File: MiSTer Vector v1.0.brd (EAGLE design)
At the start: 60.1 x 63.9 mm, 39 parts, among them CON2 22-23-2021, IC1 74HC00D, IC2 TL084, IC3 TL084, IC7 MAX6105, U1 MCP4922, U2 MCP4922, U3 MCP4922, U8 VASD1-SIP

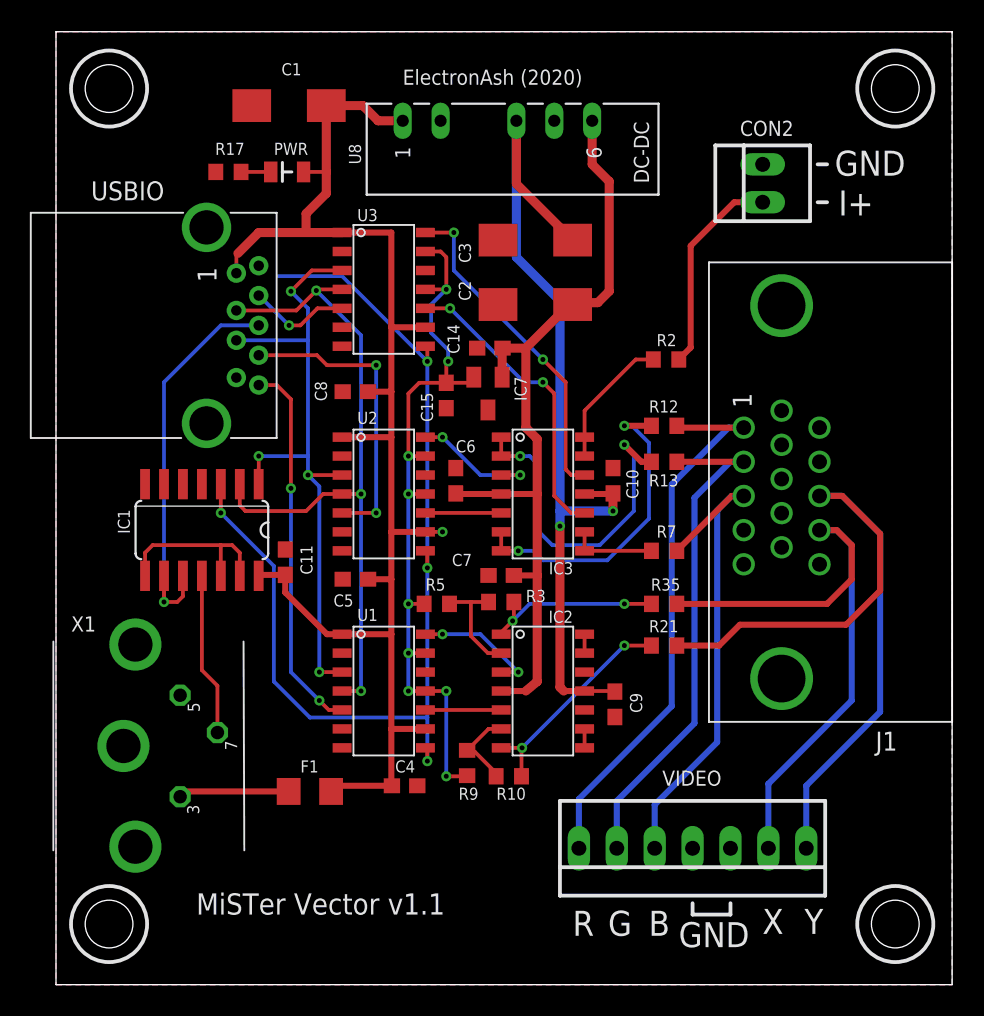
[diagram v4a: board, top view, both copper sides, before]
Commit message: changed DB15 to DB25, for use with laser projectors
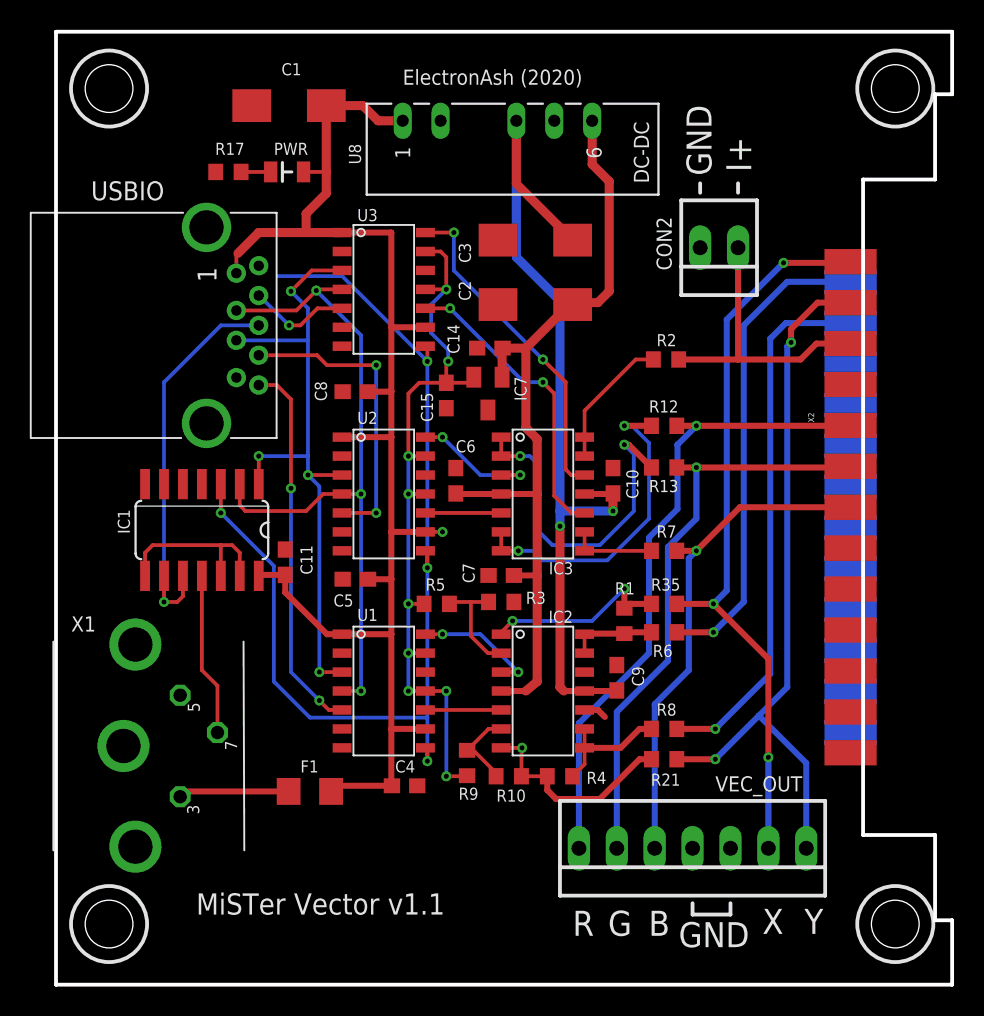
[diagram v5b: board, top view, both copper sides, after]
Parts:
- removed J1: (no value), con-wurth:618015330923
- added R1, R4: 10K, resistor:R0603
- added R6, R8: 75R, resistor:R0603
- added X2: ILDA 25 Pin, SparkFun:F25D
- moved R21 7.62 mm to (40.8, 15.1)
- moved CON2 5.21 mm to (44.5, 49.4), turned to 180 degrees
- moved C9 1.78 mm to (37.6, 20.6), turned to 270 degrees
- moved R13 0.38 mm to (40.8, 34.7)
- renumbered VIDEO to VEC_OUT
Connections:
- new net INTERLOCK: X2.17, X2.4
- new net SHUTTER: X2.13
- new net X-: R6.2, X2.14
- new net Y-: R8.2, X2.15
- net B+: now also X2.7; no longer J1.3
- net G+: now also X2.6; no longer J1.2
- net GND: now also X2.16, X2.18, X2.19, X2.20, X2.21, X2.22, X2.23, X2.25; no longer J1.10, J1.5, J1.6, J1.7, J1.8, J1.SHELL, J1.SHELL1
- net I+: now also X2.3
- net N$1: now also R1.1
- net N$2: now also R4.1
- net N$4: now also R4.2, R8.1
- net N$5: now also R1.2, R6.1
- net R+: now also X2.5; no longer J1.1
- net X+: now also X2.1; no longer J1.14
- net Y+: now also X2.2; no longer J1.13
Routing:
- net Y-: track 0.00 -> 36.1 mm, vias 0 -> 1
- net X-: track 0.00 -> 32.3 mm, vias 0 -> 1
- net N$4: track 1.27 -> 8.52 mm
- net X+: track 42.5 -> 49.7 mm, vias 0 -> 3
- net I+: track 14.0 -> 19.5 mm
- net R+: track 37.9 -> 43.2 mm, vias 0 -> 1
- net G+: track 34.4 -> 39.4 mm, vias 0 -> 1
- net N$5: track 1.27 -> 5.81 mm
- net Y+: track 52.3 -> 48.4 mm, vias 0 -> 2
- net GND: track 0.00 -> 1.55 mm
- net B+: track 32.6 -> 34.0 mm, vias 0 -> 1
- net N$1: track 12.3 -> 12.8 mm
- net N$2: track 14.8 -> 14.3 mm, vias 2 -> 1
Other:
- outline, holes or cut-outs redrawn

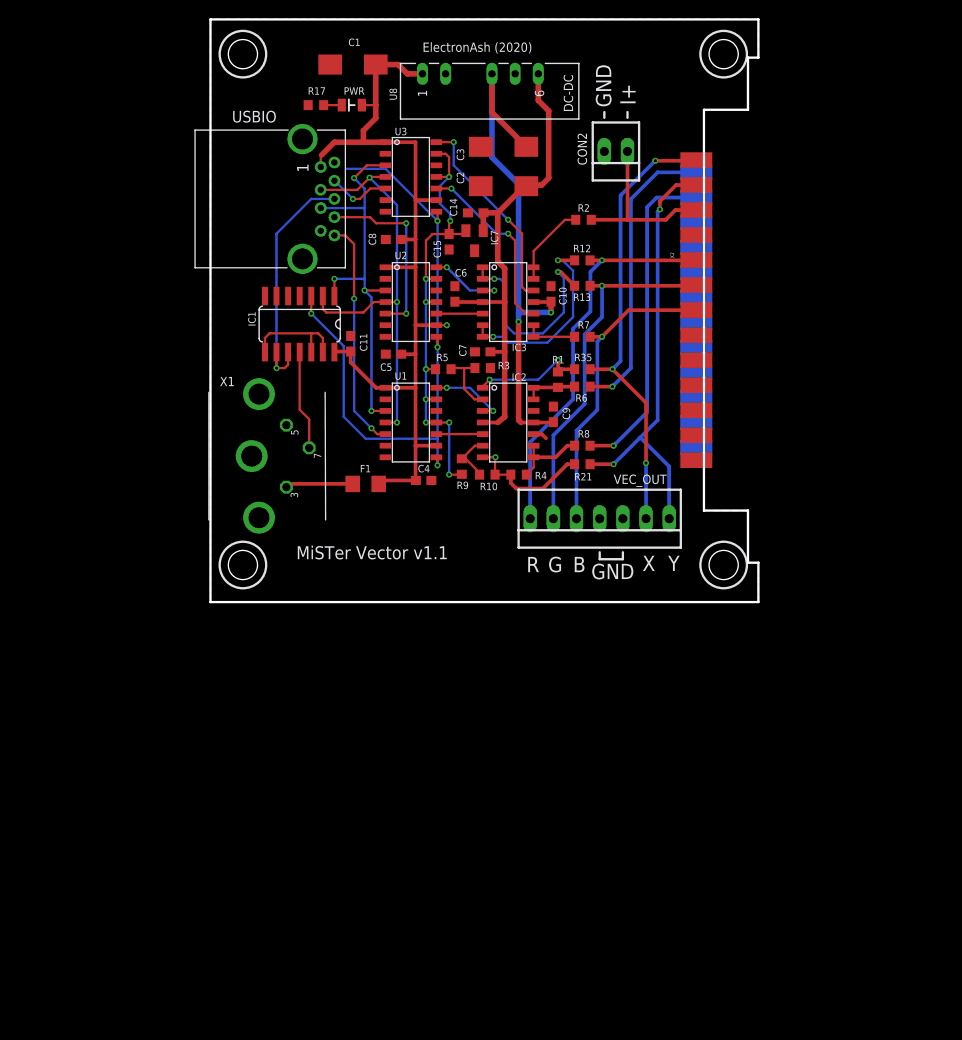
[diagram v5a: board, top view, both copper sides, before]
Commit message: made the PCB longer, to fit a specific project box
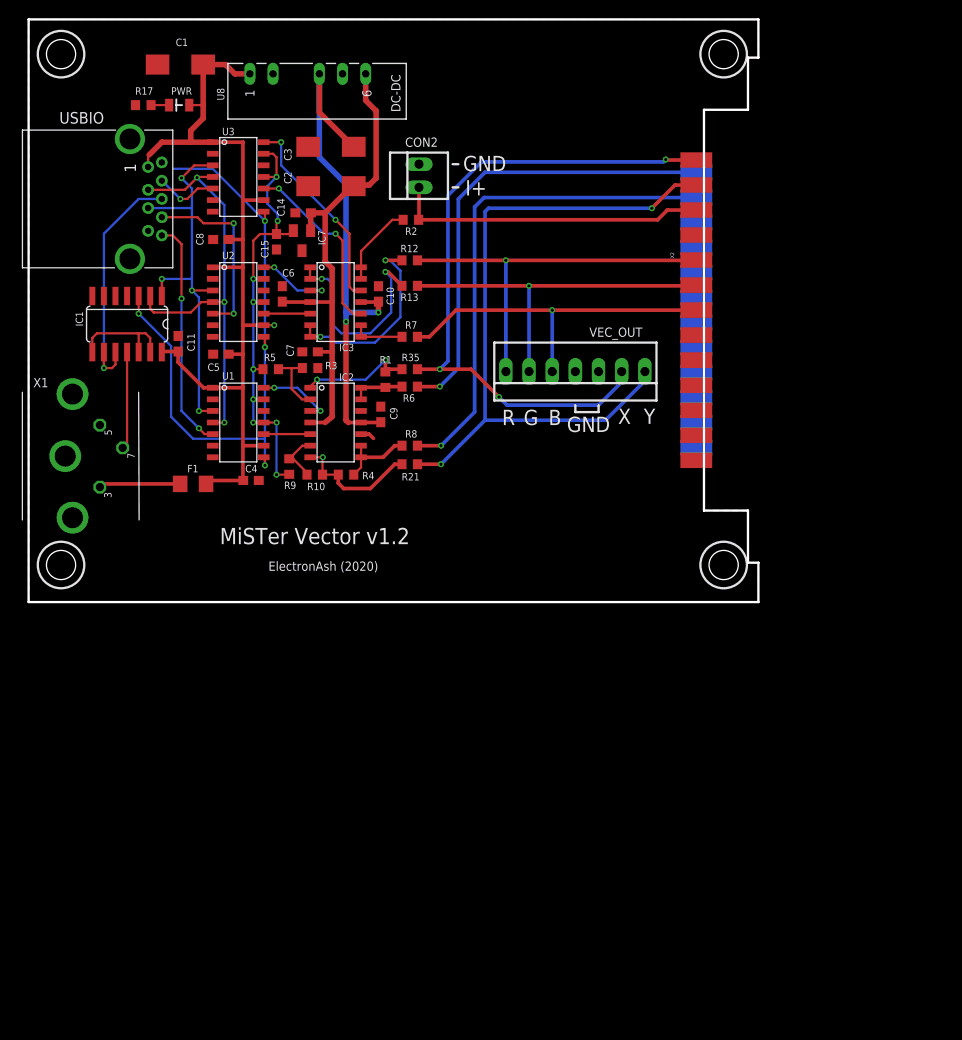
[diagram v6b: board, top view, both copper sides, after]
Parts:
- X1: value (none) -> miniDIN3
- moved CON2 21.8 mm to (22.9, 46.7), turned to 90 degrees
- moved X1 20.4 mm to (-15.9, 16.0)
- moved C1 18.9 mm to (-3.30, 58.9)
- moved C10 18.9 mm to (18.4, 33.8)
- moved C11 18.9 mm to (-3.56, 28.3)
- moved C2 18.9 mm to (13.2, 45.6)
- moved C3 18.9 mm to (13.2, 49.9)
- moved C6 18.9 mm to (7.87, 33.8)
- moved F1 18.9 mm to (-1.91, 13.0)
- moved IC1 18.9 mm to (-9.14, 30.5)
- moved IC2 18.9 mm to (11.7, 24.0)
- moved IC3 18.9 mm to (11.7, 37.2)
- moved IC7 18.9 mm to (10.0, 39.6)
- moved R1 18.9 mm to (19.2, 24.4)
- moved R10 18.9 mm to (11.4, 14.0)
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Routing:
- net Y+: track 48.4 -> 77.0 mm
- net X+: track 49.7 -> 74.5 mm
- net X-: track 32.3 -> 51.2 mm
- net Y-: track 36.1 -> 55.0 mm
- net I+: track 19.5 -> 34.5 mm
- net B+: track 34.0 -> 38.5 mm
- net N$6: track 7.42 -> 8.94 mm
- net G+: track 39.4 -> 40.0 mm
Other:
- board size 60.1 x 63.9 mm -> 80 x 63.9 mm
- board text added: "MiSTer Vector v1.2"
- board text removed: "MiSTer Vector v1.1"

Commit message: changed the miniDIN for a miniUSB, to fit the case
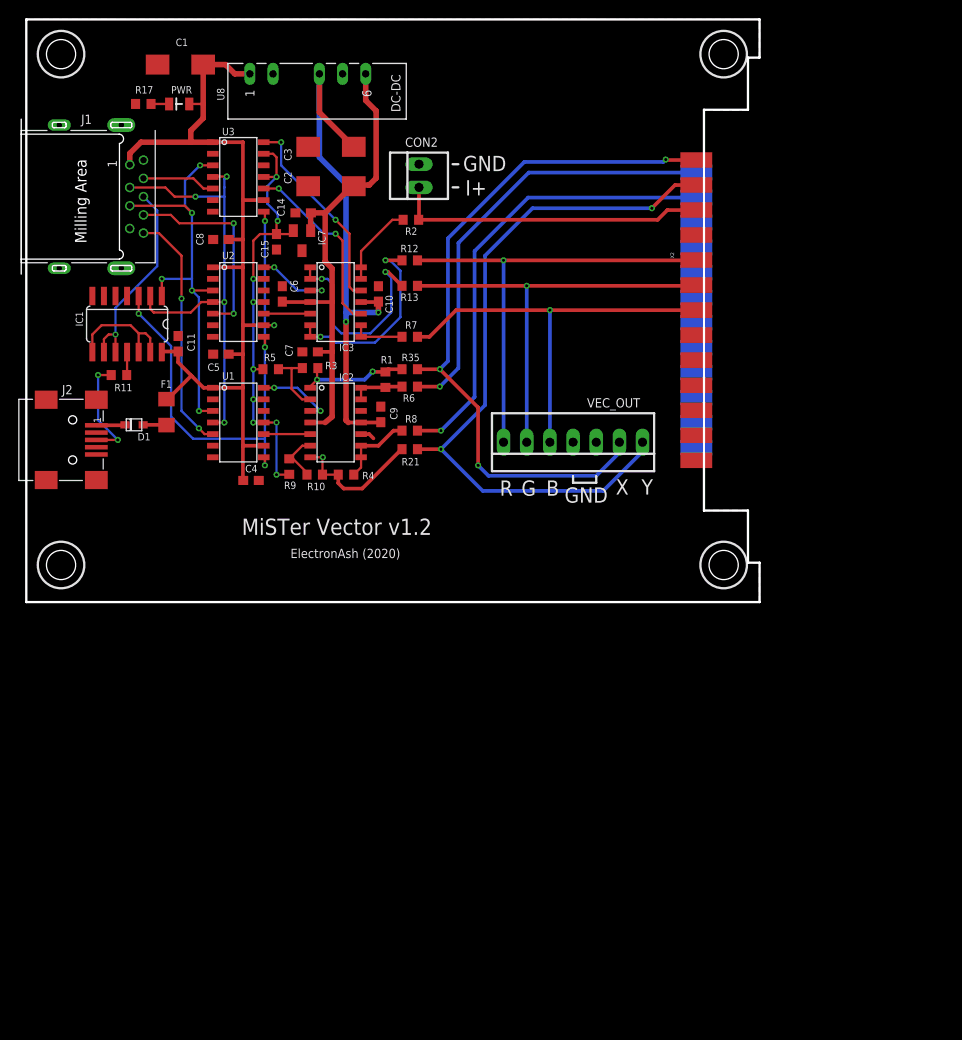
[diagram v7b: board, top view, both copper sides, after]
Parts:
- removed USBIO: (no value), con-wurth:692121030100
- removed X1: miniDIN3, mini_din:M_DIN3
- added D1: (no value), adafruit:SOD-323F
- added J1: (no value), 632723100011_Eagle_WR-USB_rev19b:692121230100
- added J2: (no value), 632723100011_Eagle_WR-USB_rev19b:65100516121
- added R11: 33R, resistor:R0603
- moved F1 8.40 mm to (-4.83, 20.8), turned to 270 degrees
- moved VEC_OUT 7.75 mm to (39.8, 17.5)
- moved R21 1.65 mm to (21.8, 16.8)
- moved R8 1.65 mm to (21.8, 18.8)
- moved PWR 0.13 mm to (-3.43, 54.6)
- moved R17 0.13 mm to (-7.37, 54.6)
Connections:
- removed net 3D_SYNC_TTL: IC1.11, X1.7
- new net N$11: D1.A, F1.2
- new net N$7: IC1.11, R11.1
- new net N$9: J2.3, R11.2
- net +3V3: now also J1.9; no longer USBIO.9
- net +5V: now also F1.1, J1.1; no longer F1.2, USBIO.1
- net 3D_SYNC_USBIO: now also J1.7; no longer USBIO.7
- net DAC_BI_DAT: now also J1.8; no longer USBIO.8
- net DAC_CS_N: now also J1.3; no longer USBIO.3
- net DAC_RG_DAT: now also J1.6; no longer USBIO.6
- net DAC_XY_DAT: now also J1.5; no longer USBIO.5
- net GND: now also J1.4, J1.SHELL, J1.SHELL1, J1.SHELL2, J1.SHELL3, J2.5, J2.SHELL, J2.SHELL1, J2.SHELL2, J2.SHELL3; no longer USBIO.4, USBIO.SHELL, USBIO.SHELL1, X1.5, X1.SH1, X1.SH2, X1.SH3
- net N$6: now also D1.C, J2.1; no longer F1.1, X1.3
- net SPI_CLK: now also J1.2; no longer USBIO.2
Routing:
- net DAC_LAT_N: track 68.6 -> 56.2 mm
- net N$9: track 0.00 -> 11.8 mm, vias 0 -> 2
- net 3D_SYNC_TTL: track 10.7 -> 0.00 mm
- net R+: track 42.8 -> 50.5 mm
- net G+: track 40.0 -> 47.7 mm
- net B+: track 38.5 -> 46.3 mm
- net N$6: track 8.94 -> 3.14 mm
- net 3D_SYNC_USBIO: track 27.2 -> 22.5 mm
- net Y-: track 55.0 -> 50.5 mm
- net X+: track 74.5 -> 78.4 mm
- net SPI_CLK: track 47.2 -> 50.9 mm, vias 3 -> 4
- net X-: track 51.2 -> 48.4 mm
- net N$11: track 0.00 -> 2.57 mm
- net N$7: track 0.00 -> 2.53 mm
- net DAC_RG_DAT: track 20.3 -> 22.5 mm
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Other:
- board size 80 x 63.9 mm -> 80.4 x 63.9 mm

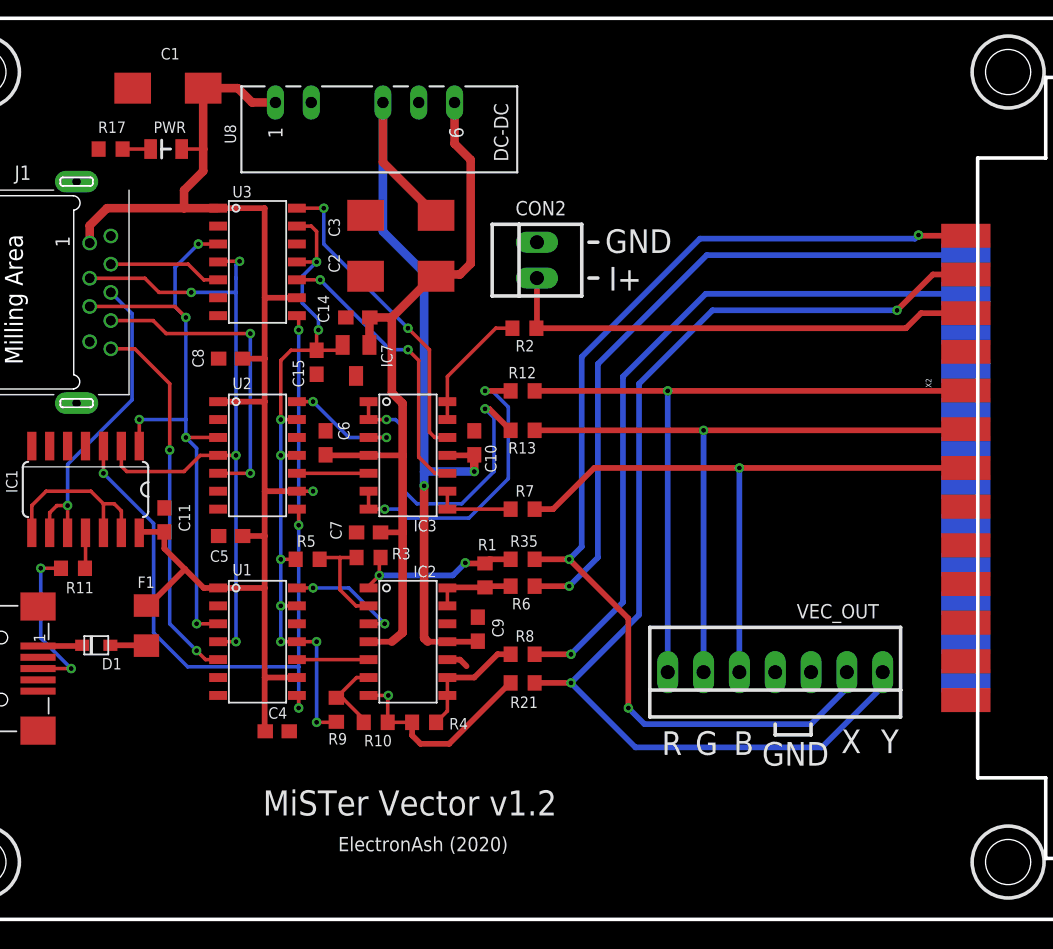
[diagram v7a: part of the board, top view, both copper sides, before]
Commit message: added VREF adj switch and pot, plus ILDA shutter jumper
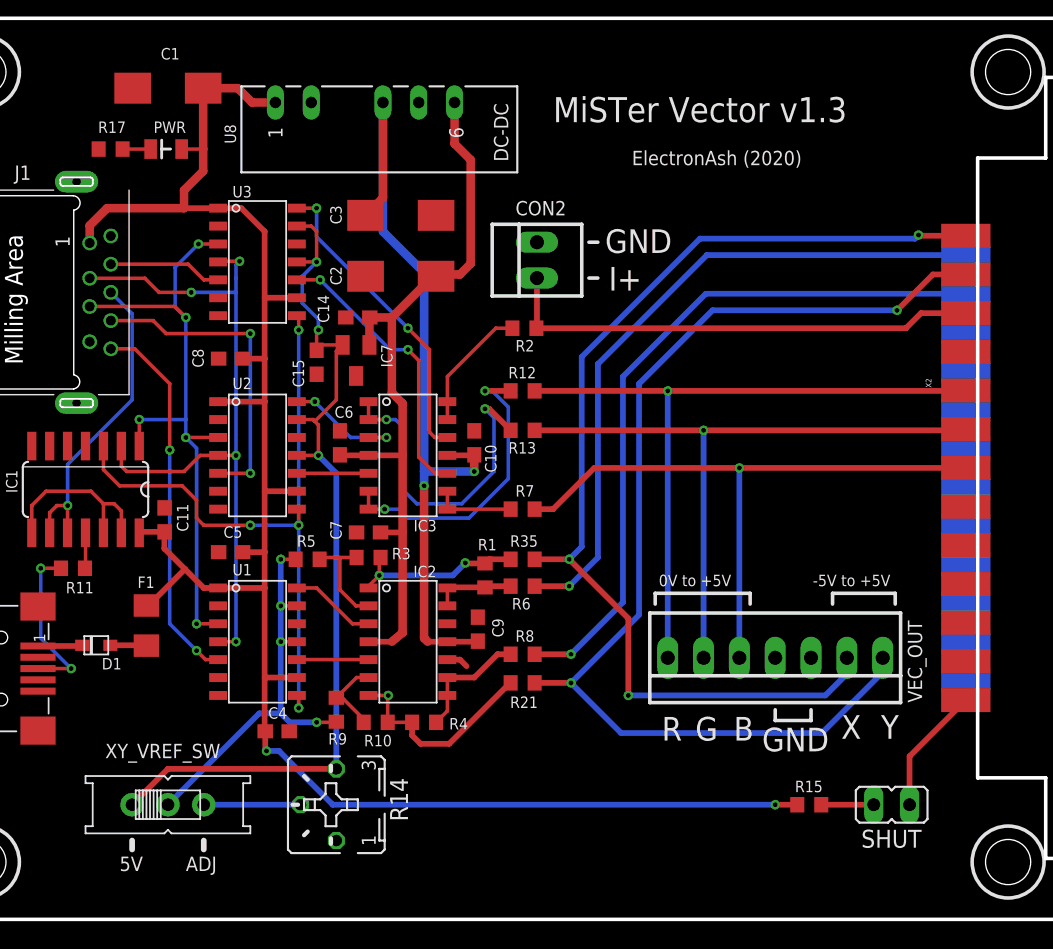
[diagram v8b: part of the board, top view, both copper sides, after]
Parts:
- added R14: (no value), pot:B25P
- added R15: 75R, resistor:R0603
- added SHUT: (no value), jumper:JP1
- added XY_VREF_SW: (no value), adafruit:EG1218
- moved C5 1.14 mm to (1.14, 26.0)
- moved VEC_OUT 1.02 mm to (39.8, 18.5)
- moved C6 1.02 mm to (8.89, 33.8)
- turned C3 to 180 degrees
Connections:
- new net +VREF_XY: R5.1, R9.1, U1.11, U1.13, XY_VREF_SW.P
- new net N$12: R15.2, SHUT.1
- new net N$13: R14.S, XY_VREF_SW.S
- net +5V: now also R15.1
- net +VREF: now also R14.E, XY_VREF_SW.O; no longer R5.1, R9.1, U1.11, U1.13
- net GND: now also R14.A
- net SHUTTER: now also SHUT.2
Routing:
- net +5V: track 96.9 -> 135.4 mm, vias 1 -> 2
- net +VREF_XY: track 0.00 -> 29.2 mm, vias 0 -> 4
- net +VREF: track 51.4 -> 64.3 mm, vias 9 -> 3
- net SHUTTER: track 0.00 -> 9.07 mm
- net DAC_LAT_N: track 56.2 -> 48.1 mm
- net N$13: track 0.00 -> 6.86 mm
- net N$12: track 0.00 -> 3.72 mm
- net DACX: track 8.42 -> 6.13 mm, vias 2 -> 0
- net X+: track 78.4 -> 76.7 mm
- net -12V: track 59.3 -> 58.3 mm
- net B+: track 46.3 -> 45.2 mm
- net R+: track 50.5 -> 49.5 mm
- net G+: track 47.7 -> 46.7 mm
- net +12V: track 55.8 -> 54.8 mm
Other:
- board text added: "-5V to +5V"
- board text added: "0V to +5V"
- board text added: "ADJ"
- board text added: "MiSTer Vector v1.3"
- board text removed: "MiSTer Vector v1.2"
